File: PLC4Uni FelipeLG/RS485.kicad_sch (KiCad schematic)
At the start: 5 parts, among them U5 SP3485EN

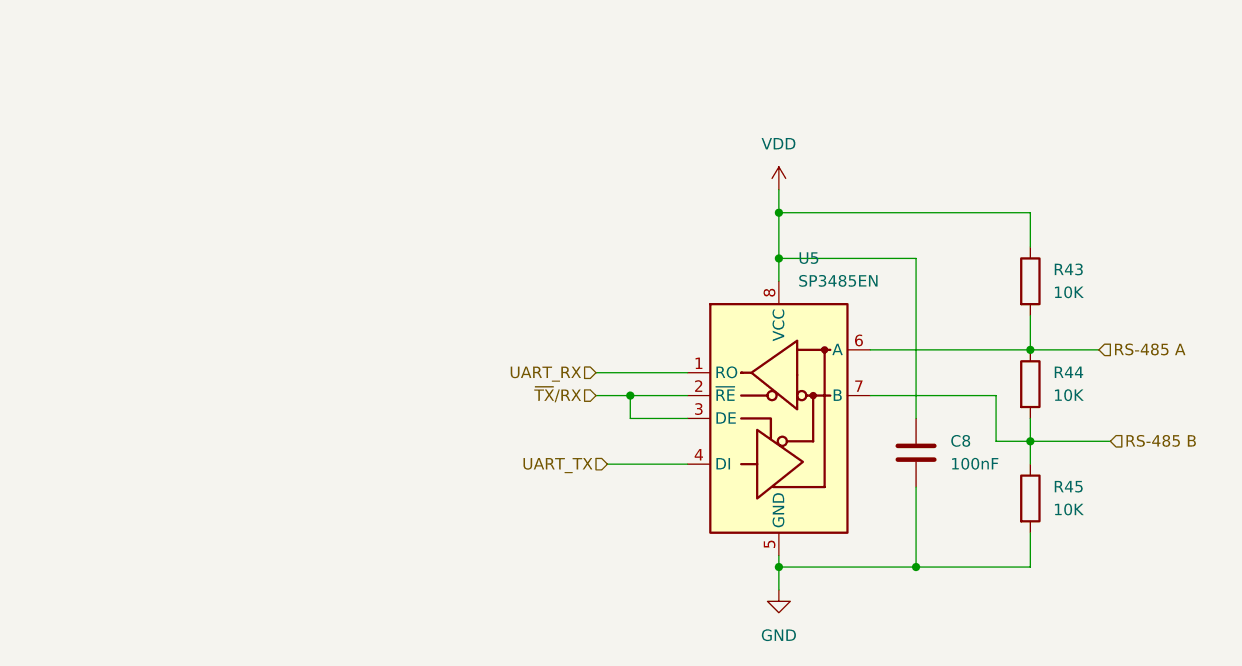
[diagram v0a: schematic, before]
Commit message: Add files via upload
Updated Circuitos corregidos y pistas agregadas
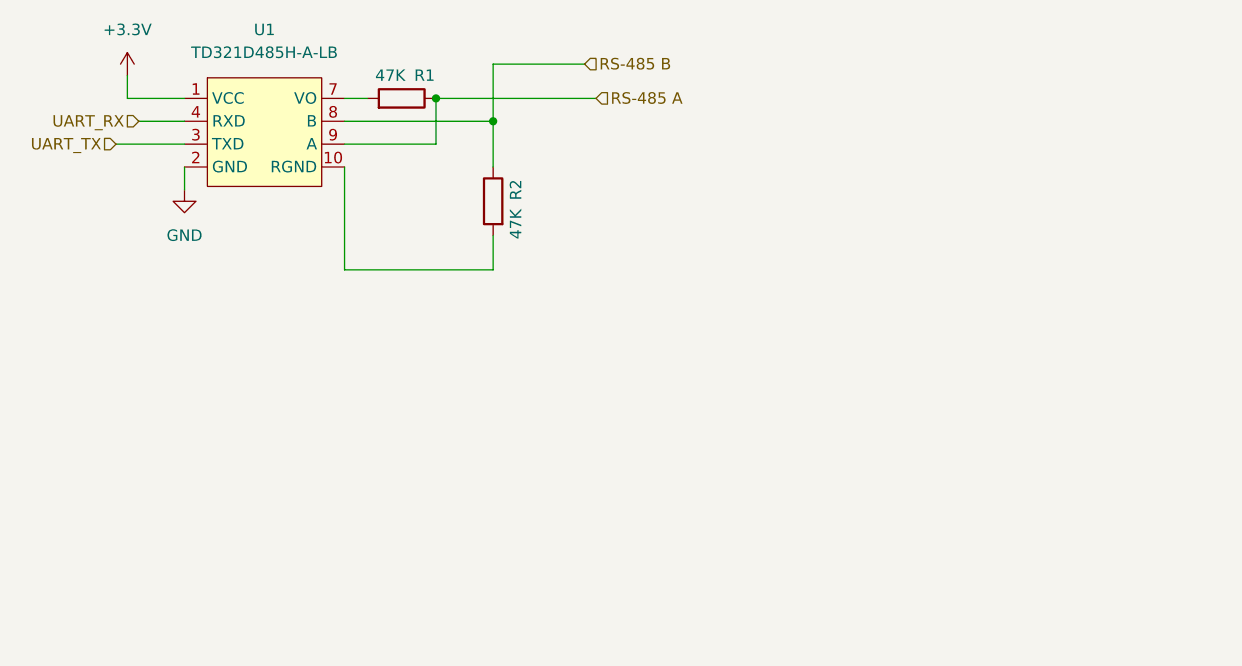
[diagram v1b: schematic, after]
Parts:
- removed C8: 100nF, Capacitor_SMD:C_0201_0603Metric, symbol Device:C
- removed R43, R44, R45: 10K, PCM_Resistor_SMD_AKL:R_0603_1608Metric, symbol Device:R
- removed U5: SP3485EN, Package_SO:SOIC-8_3.9x4.9mm_P1.27mm, symbol Interface_UART:SP3485EN
- added R1, R2: 47K, Resistor_SMD_AKL:R_0603_1608Metric, symbol PCM_Resistor_AKL:R_0603
- added U1: TD321D485H-A-LB, Custom_Footprint:TD321D48H-A, symbol RS_485_BUS_MODULE:TD321D485H-A-LB
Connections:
- net GND: now also U1.2 (GND)
- net RS-485 A: now also R1.2, U1.9 (A)
- net RS-485 B: now also R2.2, U1.8 (B)
- net UART_RX: now also U1.4 (RXD)
- net UART_TX: now also U1.3 (TXD)
- new net: R2.1, U1.10 (RGND)
- new net: R1.1, U1.7 (VO)
- new net +3.3V: U1.1 (VCC)
